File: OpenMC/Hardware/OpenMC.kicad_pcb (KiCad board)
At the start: 2 copper layers, 50.8 x 63.5 mm, 65 parts, among them IC1 ESP32-C3, IC2 INA186A4QDBVRQ1, IC3 INA186A4QDBVRQ1, IC4 INA186A4QDBVRQ1, J1 Conn_01x01_Female, J2 Conn_01x01_Female, J3 Power+, J4 Conn_01x04_Female, J5 Power-, J6 Conn_01x01_Female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

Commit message: updated mc
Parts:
- IC1: footprint SamacSys_Parts:QFN50P500X500X90-33N-D -> Package_DFN_QFN:HVQFN-32-1EP_5x5mm_P0.5mm_EP3.1x3.1mm
- J4: value Conn_01x04_Female -> Comm
- Y1: footprint SamacSys_Parts:ABM12W300000MHZ6B1UT3 -> Crystal:Crystal_SMD_SeikoEpson_TSX3225-4Pin_3.2x2.5mm
- moved C10 20.6 mm to (151.0, 142.1), turned to -90 degrees
- moved Y1 1.27 mm to (131.5, 133.8)
- moved Q9 0.15 mm to (120.0, 99.8)
- moved Q11 0.10 mm to (125.7, 99.8)
- moved R12 0.06 mm to (126.0, 122.9)
- moved R10 0.06 mm to (128.3, 122.9)
- moved R4 0.06 mm to (140.5, 122.9)
- moved R6 0.06 mm to (138.2, 122.9)
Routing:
- net /Pre-Driver/V_{DRIVE}: track 56.2 -> 62.9 mm, vias 4 -> 2
- net Net-(IC1-Pad30): track 4.08 -> 7.81 mm
- net /VDD: track 159.2 -> 162.3 mm
- net /Driver FETs/BH: track 38.6 -> 36.3 mm
- net Earth: vias 30 -> 13
- net /C: vias 108 -> 104
- net /B: vias 108 -> 104
- net /A: vias 100 -> 96
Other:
- board text added: "A"
- board text added: "B"
- board text added: "C"

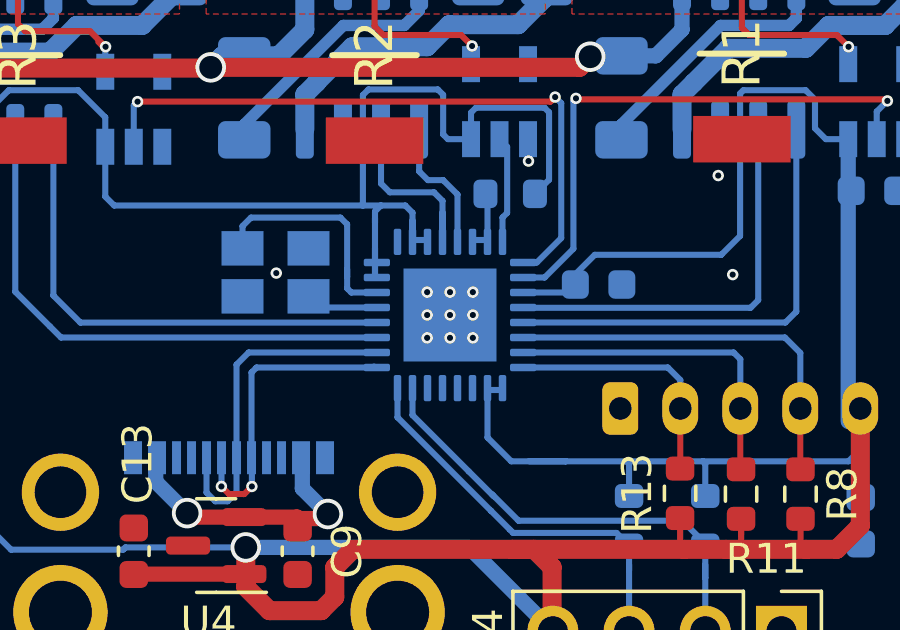
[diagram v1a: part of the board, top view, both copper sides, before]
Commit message: updated footprint
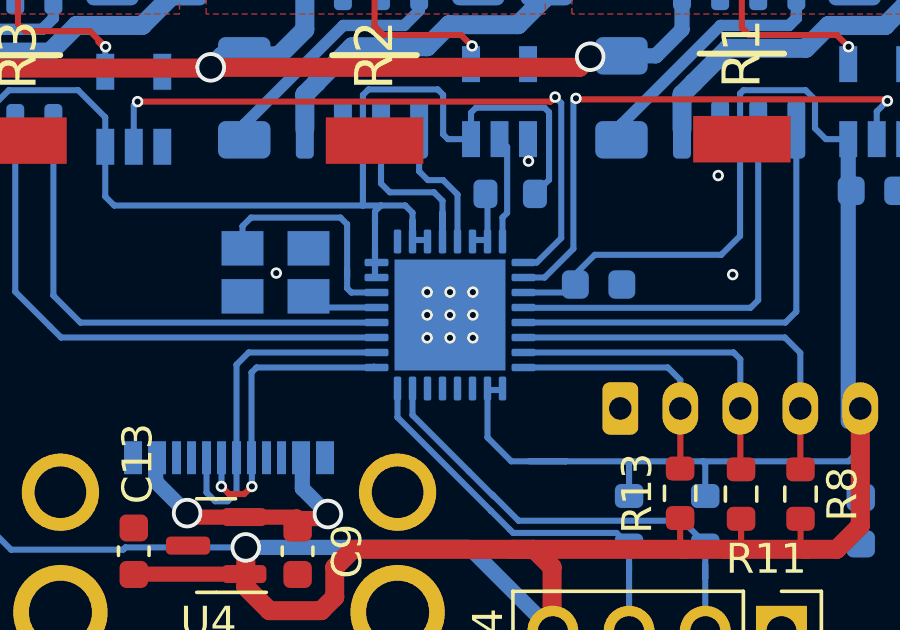
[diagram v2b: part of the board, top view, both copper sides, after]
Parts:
- IC1: footprint Package_DFN_QFN:HVQFN-32-1EP_5x5mm_P0.5mm_EP3.1x3.1mm -> Package_DFN_QFN:QFN-32-1EP_5x5mm_P0.5mm_EP3.7x3.7mm
